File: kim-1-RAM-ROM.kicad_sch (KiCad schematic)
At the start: 41 parts, among them J1 Conn_03x08, J2 Conn_03x06, J3 Conn_02x08_Counter_Clockwise, SW1 Vectors, SW2 SW_DIP_x08, SW3 SW_DIP_x07, SW4 SW_DIP_x01, SW5 SW_DIP_x01, SW6 Image_set, U1 74LS04, U10 SST39SF020, U11 628128, U2 74LS08, U3 74LS08, U4 74HCT541, U5 74HCT541, U6 74LS133, U7 74LS145, U8 74LS145, U9 74LS145, X1 EDGE_CONN

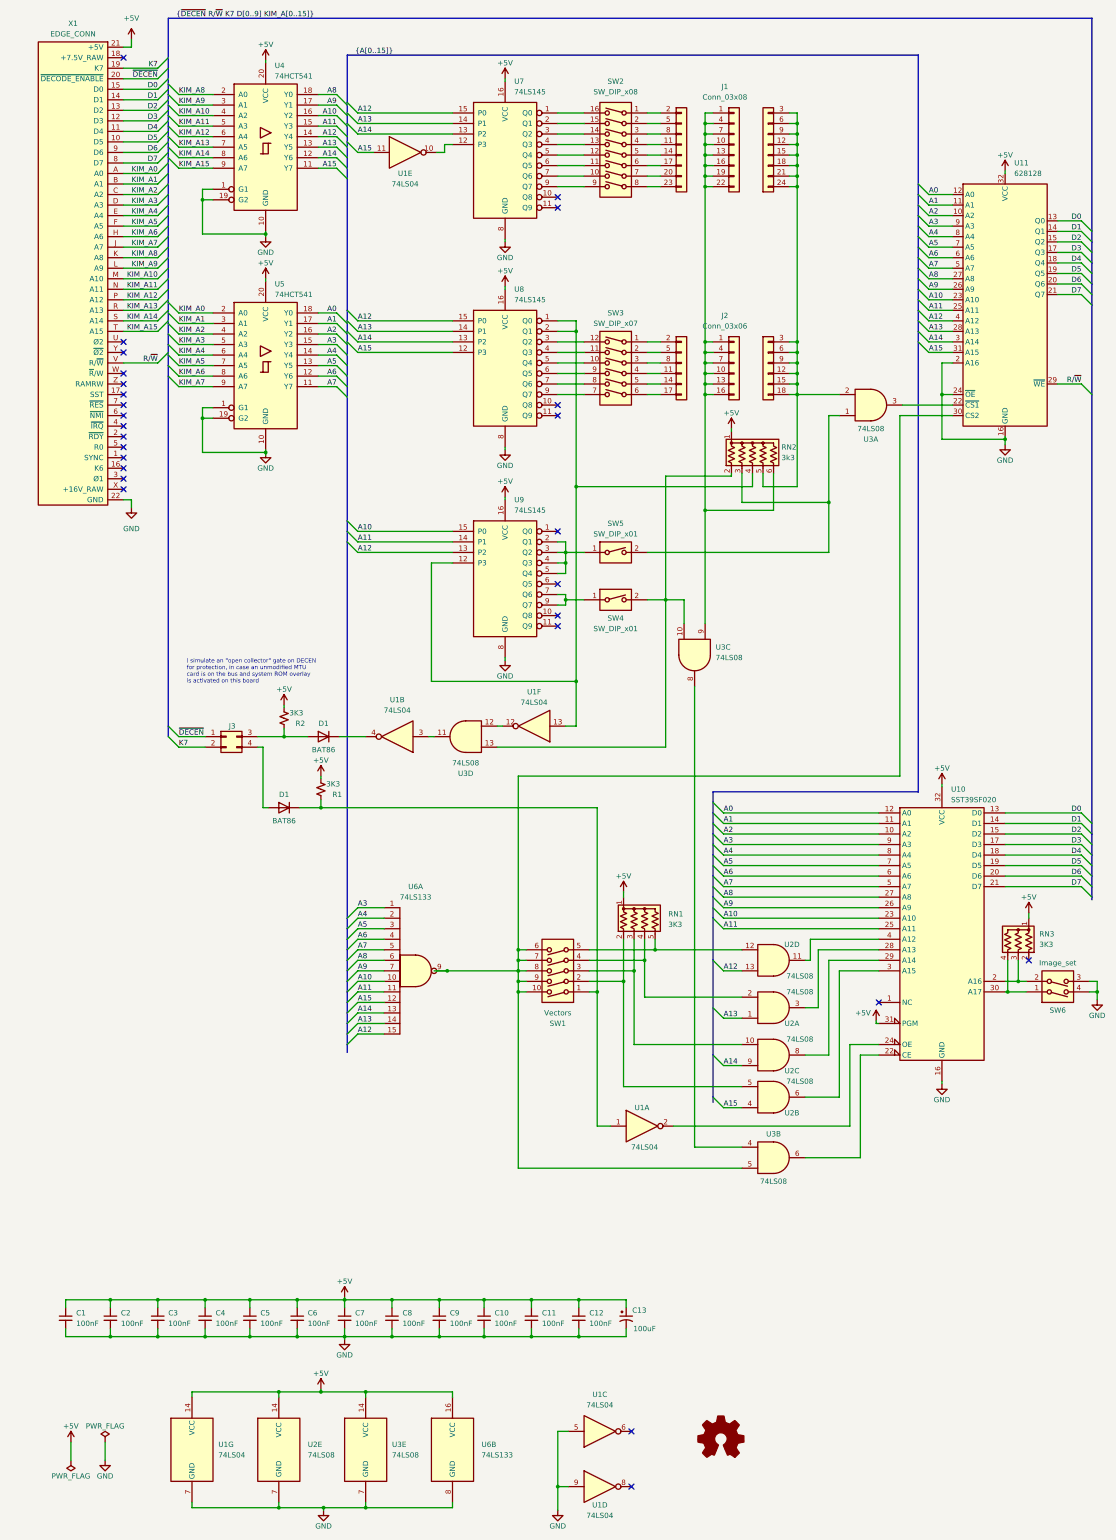
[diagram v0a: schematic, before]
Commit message: Add option to support the MTU floppy controller boot prom
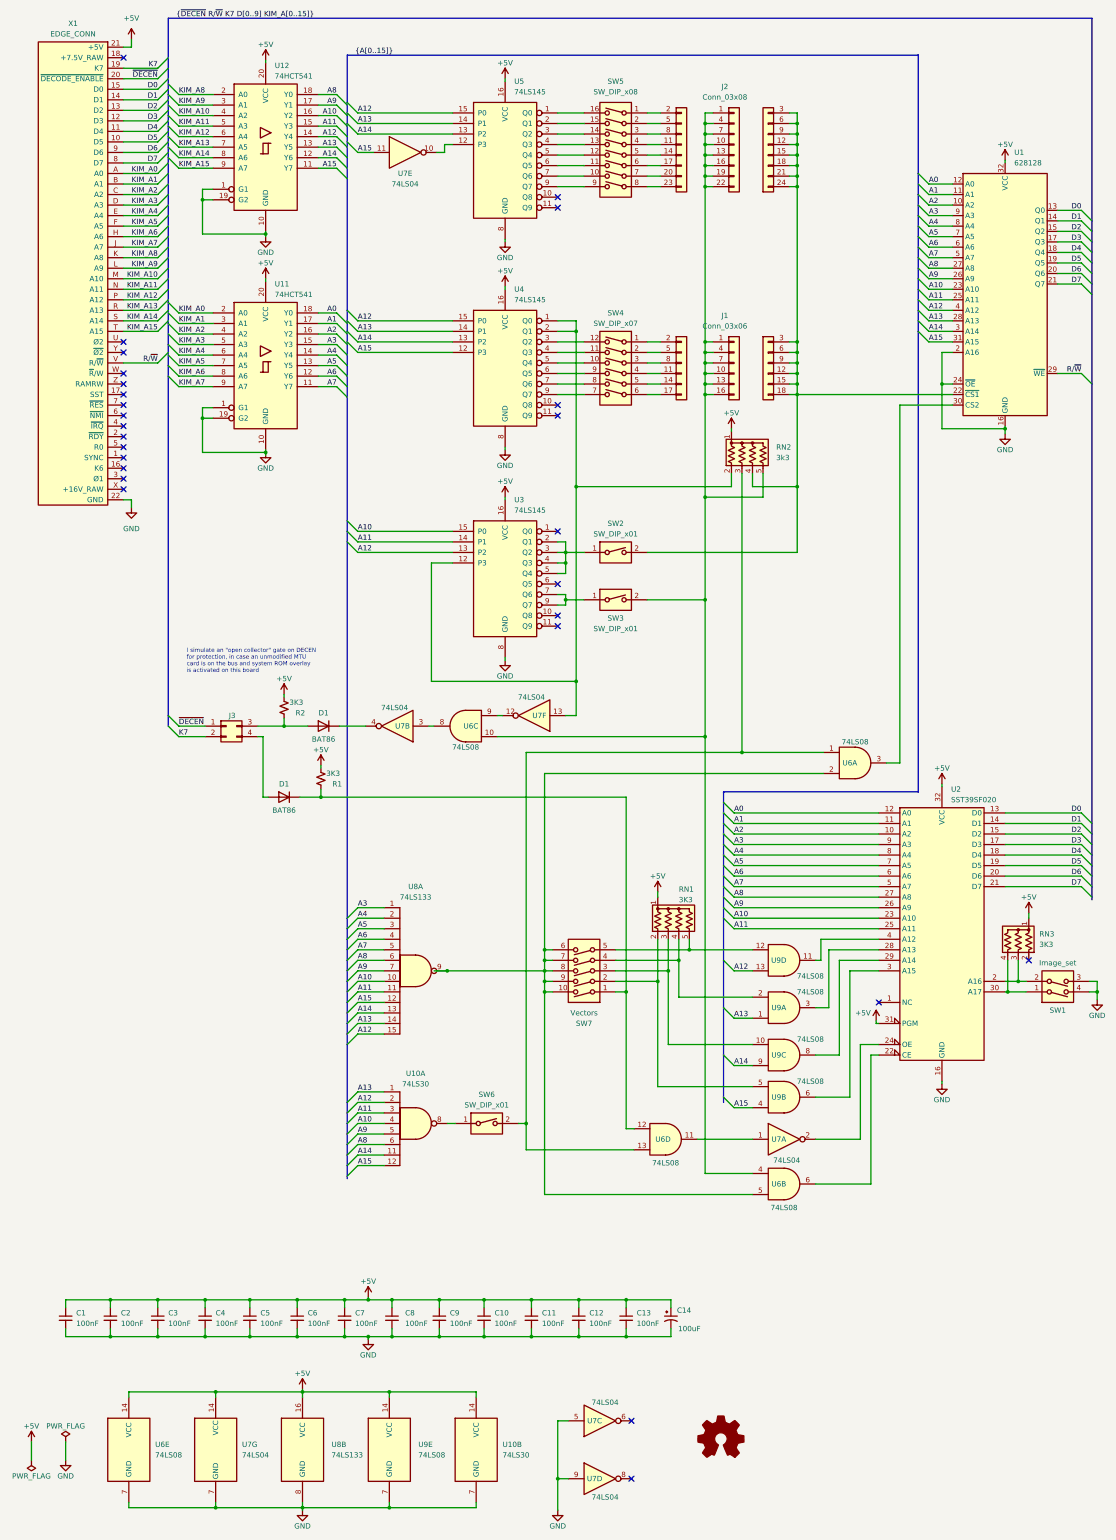
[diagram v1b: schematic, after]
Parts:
- removed unit 3 of U3
- removed unit 1 of U3
- added C10: 100nF, Capacitor_THT:C_Disc_D5.0mm_W2.5mm_P5.00mm, symbol Device:C_Small
- added SW6: SW_DIP_x01, Button_Switch_THT:SW_DIP_SPSTx01_Slide_9.78x4.72mm_W7.62mm_P2.54mm, symbol Switch:SW_DIP_x01
- added U10: 74LS30, Package_DIP:DIP-14_W7.62mm_LongPads, symbol 74xx:74LS30
- added unit 4 of U6
- added unit 1 of U6
- RN2: footprint Resistor_THT:R_Array_SIP6 -> Resistor_THT:R_Array_SIP5; symbol Device:R_Network05_US -> Device:R_Network04_US
- renumbered C11 to C1, C5 to C11, C4 to C12, C12 to C13, C13 to C14, C10 to C2, C9 to C3, C8 to C4, C7 to C5, C3 to C6, C1 to C7, C6 to C8, C2 to C9, J2 to J1, J1 to J2, SW6 to SW1, SW5 to SW2, SW4 to SW3, SW3 to SW4, SW2 to SW5, SW1 to SW7, U11 to U1, U5 to U11, U4 to U12, U10 to U2, U9 to U3, U8 to U4, U7 to U5, U3 to U6, U1 to U7, U6 to U8, U2 to U9
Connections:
- net +5V: now also C10.1, U10.14 (VCC)
- net A10: now also U10.4
- net A11: now also U10.3
- net A12: now also U10.2
- net A13: now also U10.1
- net A14: now also U10.11
- net A15: now also U10.12
- net A8: now also U10.6
- net A9: now also U10.5
- net GND: now also C10.2, U10.7 (GND)
- net at D1.1 (K), R1.1, SW7.1: now also U6.12; no longer U7.1
- net at U6.4: now also J1.1 (Pin_1), J1.10 (Pin_10), J1.13 (Pin_13), J1.16 (Pin_16), J1.4 (Pin_4), J1.7 (Pin_7), J2.1 (Pin_1), J2.10 (Pin_10), J2.13 (Pin_13), J2.16 (Pin_16), J2.19 (Pin_º9), J2.22 (Pin_22), J2.4 (Pin_4), J2.7 (Pin_7), RN2.5 (R4), SW3.2, U6.10
- net at RN2.3 (R2): now also SW6.2, U6.1, U6.13; no longer SW2.2
- net at U3.12 (P3), U4.1 (Q0), U4.2 (Q1)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: now also RN2.2 (R1); no longer RN2.4 (R3)
- net at J1.12 (Pin_12), J1.15 (Pin_15), J1.18 (Pin_18)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: now also RN2.4 (R3), SW2.2, U1.22 (~{CS1}); no longer RN2.5 (R4)
- net at U7.3: now also U6.8; no longer U6.11
- net at U7.12: now also U6.9; no longer U6.12
- net at SW7.10, SW7.6, SW7.7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: now also U6.2; no longer U1.30 (CS2)
- new net: U6.11, U7.1
- new net: SW6.1, U10.8
- new net: U1.30 (CS2), U6.3
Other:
- moved on the sheet: C1, C11, C12, C13, C14, C2, C3, C4, C5, C6, C7, C8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

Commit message: Remove useless switch and simplify design
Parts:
- removed C10: 100nF, Capacitor_THT:C_Disc_D5.0mm_W2.5mm_P5.00mm, symbol Device:C_Small
- removed SW6: SW_DIP_x01, Button_Switch_THT:SW_DIP_SPSTx01_Slide_9.78x4.72mm_W7.62mm_P2.54mm, symbol Switch:SW_DIP_x01
- removed U10: 74LS30, Package_DIP:DIP-14_W7.62mm_LongPads, symbol 74xx:74LS30
- removed unit 1 of U6
- added unit 3 of U6
- RN2: footprint Resistor_THT:R_Array_SIP5 -> Resistor_THT:R_Array_SIP4; symbol Device:R_Network04_US -> Device:R_Network03_US
- renumbered C11 to C10, C12 to C11, C13 to C12, C14 to C13, SW7 to SW6, U11 to U10, U12 to U11
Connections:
- net A15: now also U9.5; no longer U9.4
- net GND: now also U6.12, U6.13, U6.10, U6.9
- net at D1.1 (K), R1.1, SW6.1: now also U7.1; no longer U6.12
- net at RN1.2 (R1), SW6.2: now also U9.4; no longer U9.5
- net at RN2.3 (R2): now also J1.12 (Pin_12), J1.15 (Pin_15), J1.18 (Pin_18), J1.3 (Pin_3), J1.6 (Pin_6), J1.9 (Pin_9), J2.12 (Pin_12), J2.15 (Pin_15), J2.18 (Pin_18), J2.21 (Pin_21), J2.24 (Pin_24), J2.3 (Pin_3), J2.6 (Pin_6), J2.9 (Pin_9), SW2.2, U1.22 (~{CS1}); no longer U6.13
- net at J1.1 (Pin_1), J1.10 (Pin_10), J1.13 (Pin_13)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: now also RN2.4 (R3), U6.1, U6.4; no longer RN2.5 (R4), U6.10, U6.4
- net at U6.11: no longer U7.1
- net at U7.3: now also U6.6; no longer U6.8
- net at U7.12: now also U6.5; no longer U6.9
- net at SW6.10, SW6.6, SW6.7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: now also U1.30 (CS2), U6.2; no longer U6.5
- net at U2.22 (CE): now also U6.3; no longer U6.6
- no-connect marks 27 -> 29
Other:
- moved on the sheet: C10, C11, C12, C13, U6B, U7C, U7D

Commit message: Release 2.0. Fixes issue #1
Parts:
- removed SW2, SW3: SW_DIP_x01, Button_Switch_THT:SW_DIP_SPSTx01_Slide_9.78x4.72mm_W7.62mm_P2.54mm, symbol Switch:SW_DIP_x01
- added SW2: SW_DIP_x03, Button_Switch_THT:SW_DIP_SPSTx03_Slide_9.78x9.8mm_W7.62mm_P2.54mm, symbol Switch:SW_DIP_x03
- RN2: value 3k3 -> 3K3
- renumbered SW4 to SW3, SW5 to SW4, SW6 to SW5
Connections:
- net GND: no longer U6.12, U6.13
- net at J1.12 (Pin_12), J1.15 (Pin_15), J1.18 (Pin_18)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: now also U6.13, SW2.5, SW2.6
- net at J1.1 (Pin_1), J1.10 (Pin_10), J1.13 (Pin_13)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: now also U6.12, SW2.4; no longer U6.4
- net at U3.1 (Q0): now also SW2.1
- net at U3.2 (Q1), U3.3 (Q2), U3.4 (Q3)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: now also SW2.2
- net at U3.7 (Q6), U3.9 (Q7): now also SW2.3
- net at U6.11: now also U6.4
- no-connect marks 29 -> 27
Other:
- moved on the sheet: U6D

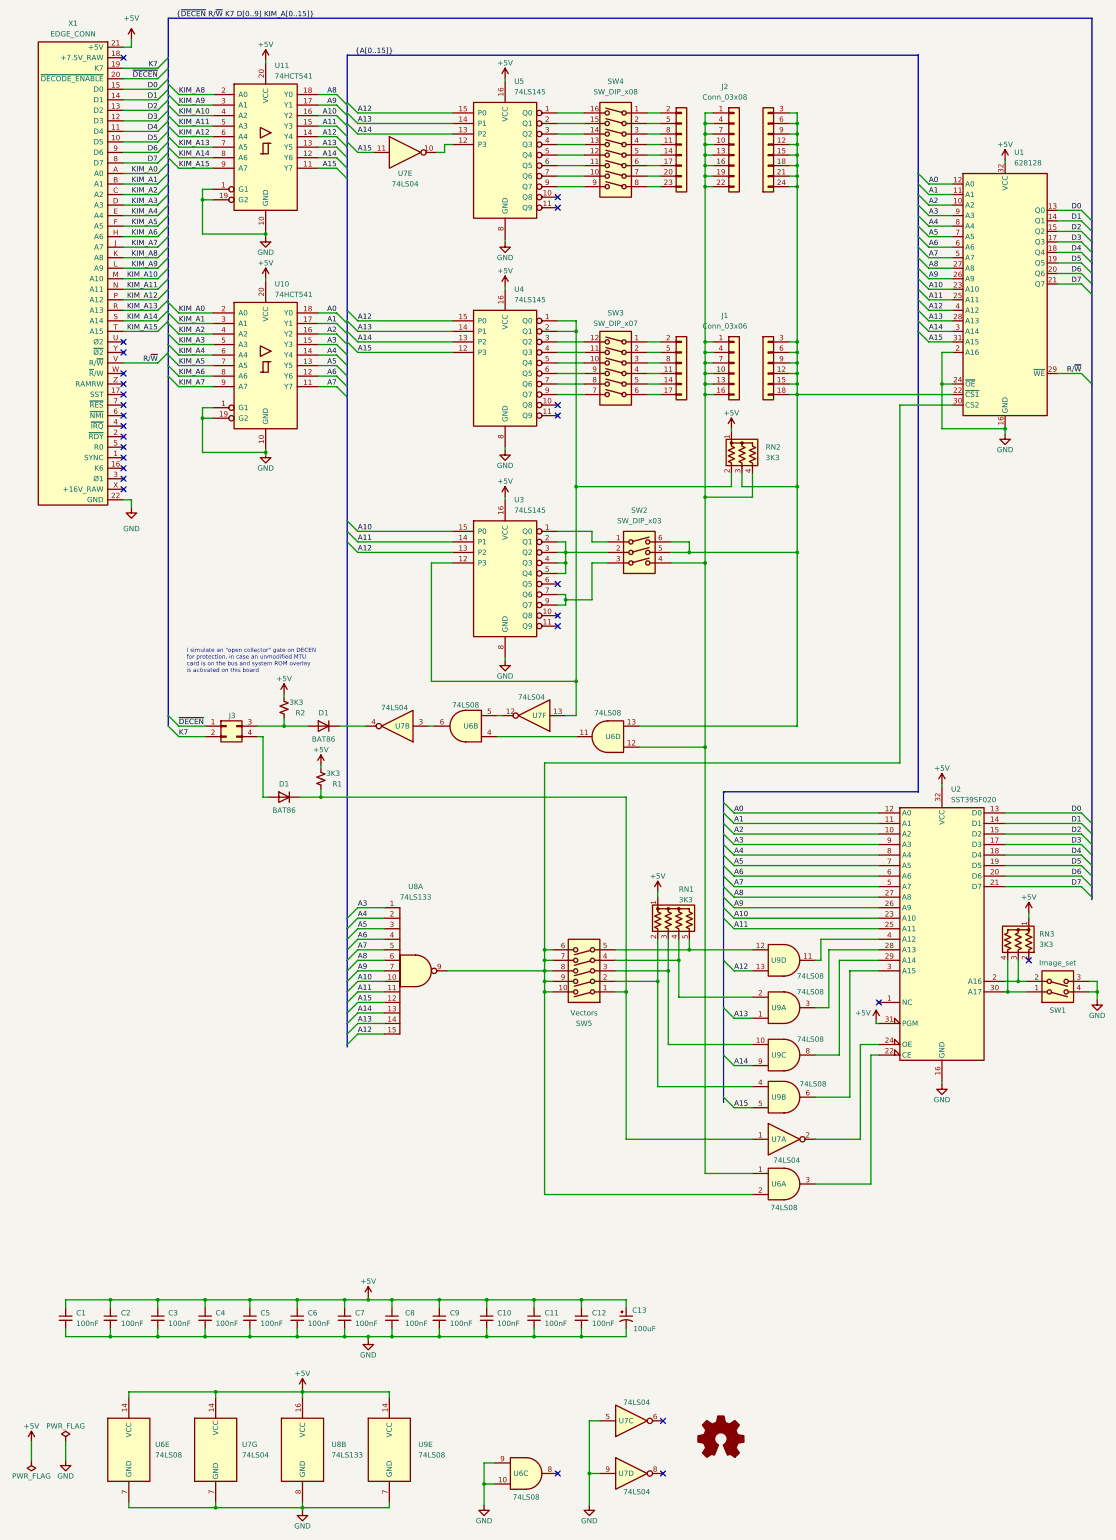
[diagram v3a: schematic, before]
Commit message: Fix replacing system RAM
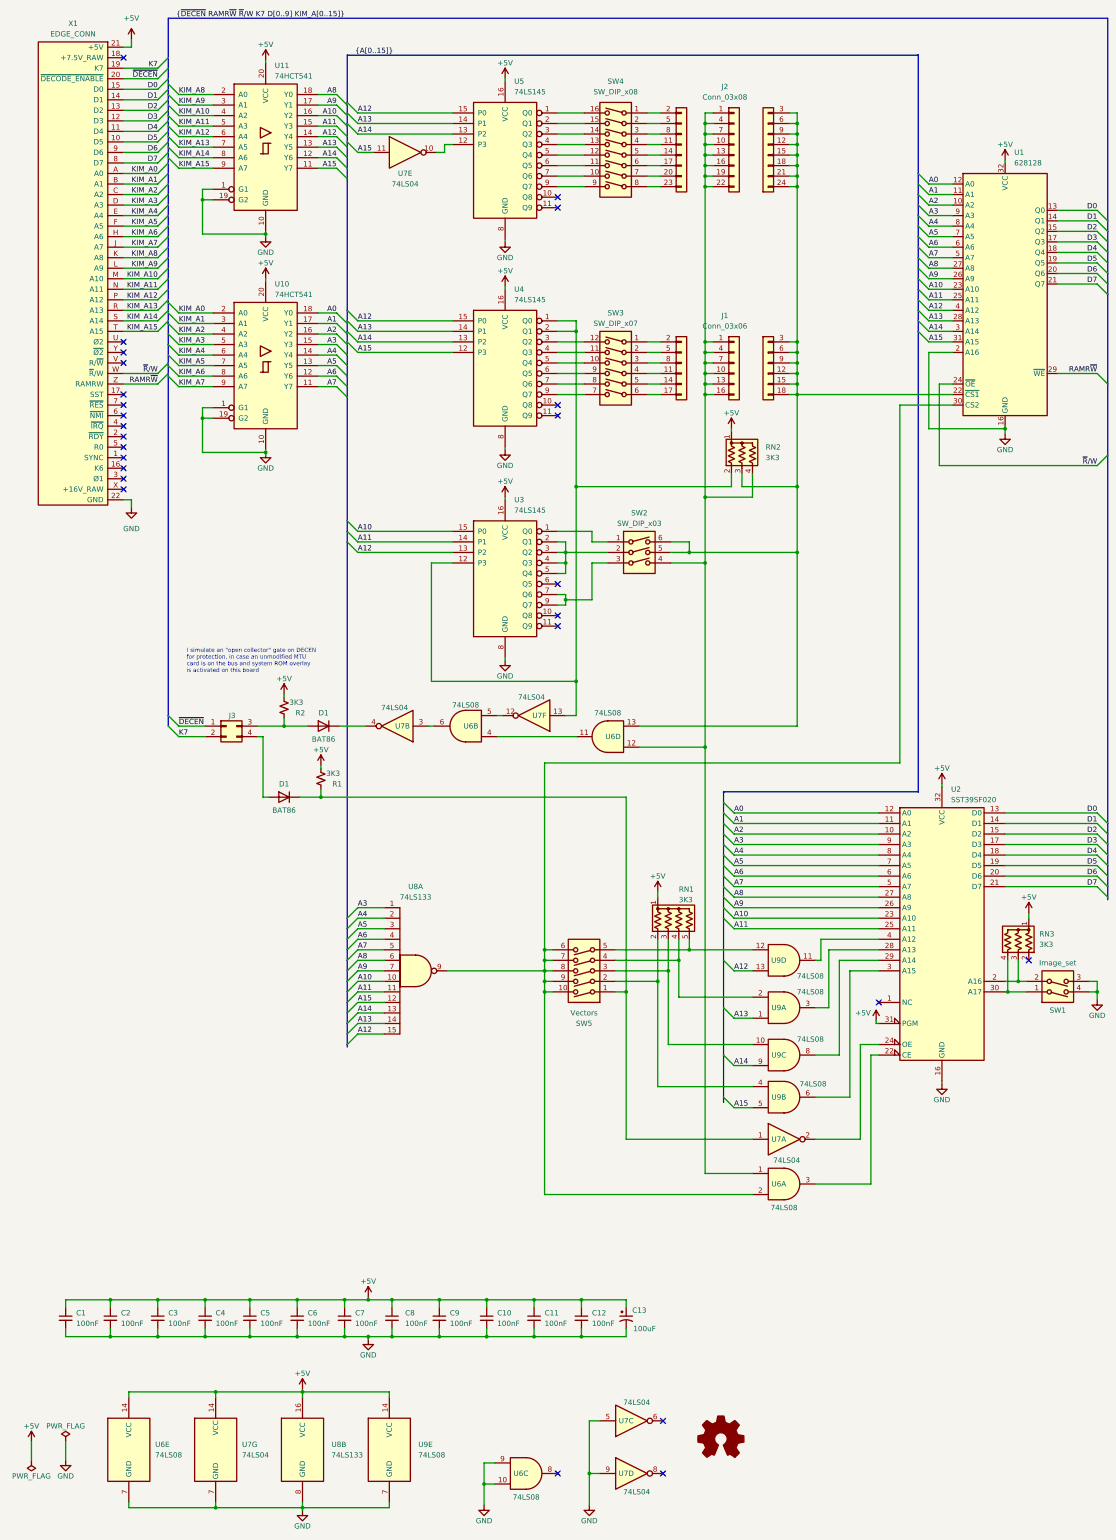
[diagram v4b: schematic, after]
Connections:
- net GND: no longer U1.24 (~{OE})
- net ~{R}/W: now reaches X1.W (~{R}/W)
- net ~{R}/W: now also U1.24 (~{OE})
- net RAMR~{W}: now reaches X1.Z (RAMRW)
- net RAMR~{W}: now also U1.29 (~{WE})
- net R/~{W}: no longer names the net of X1.V (R/~{W})
- net R/~{W}: no longer U1.29 (~{WE})
- no-connect marks 27 -> 26
